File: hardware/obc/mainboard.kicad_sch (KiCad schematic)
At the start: 0 parts

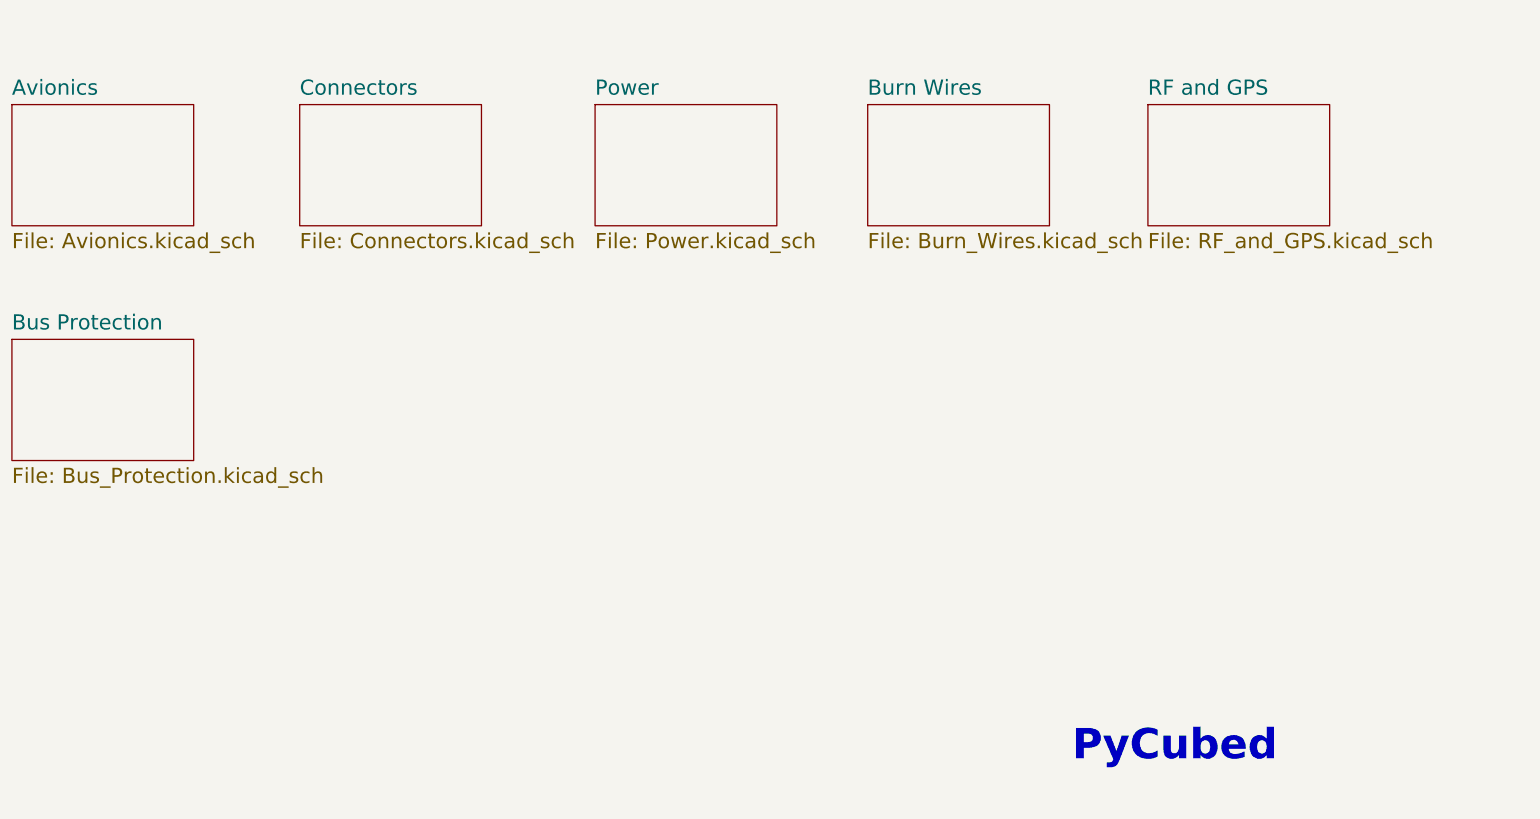
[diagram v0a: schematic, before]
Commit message: obc: Schematic pages to US Letter (except Power)
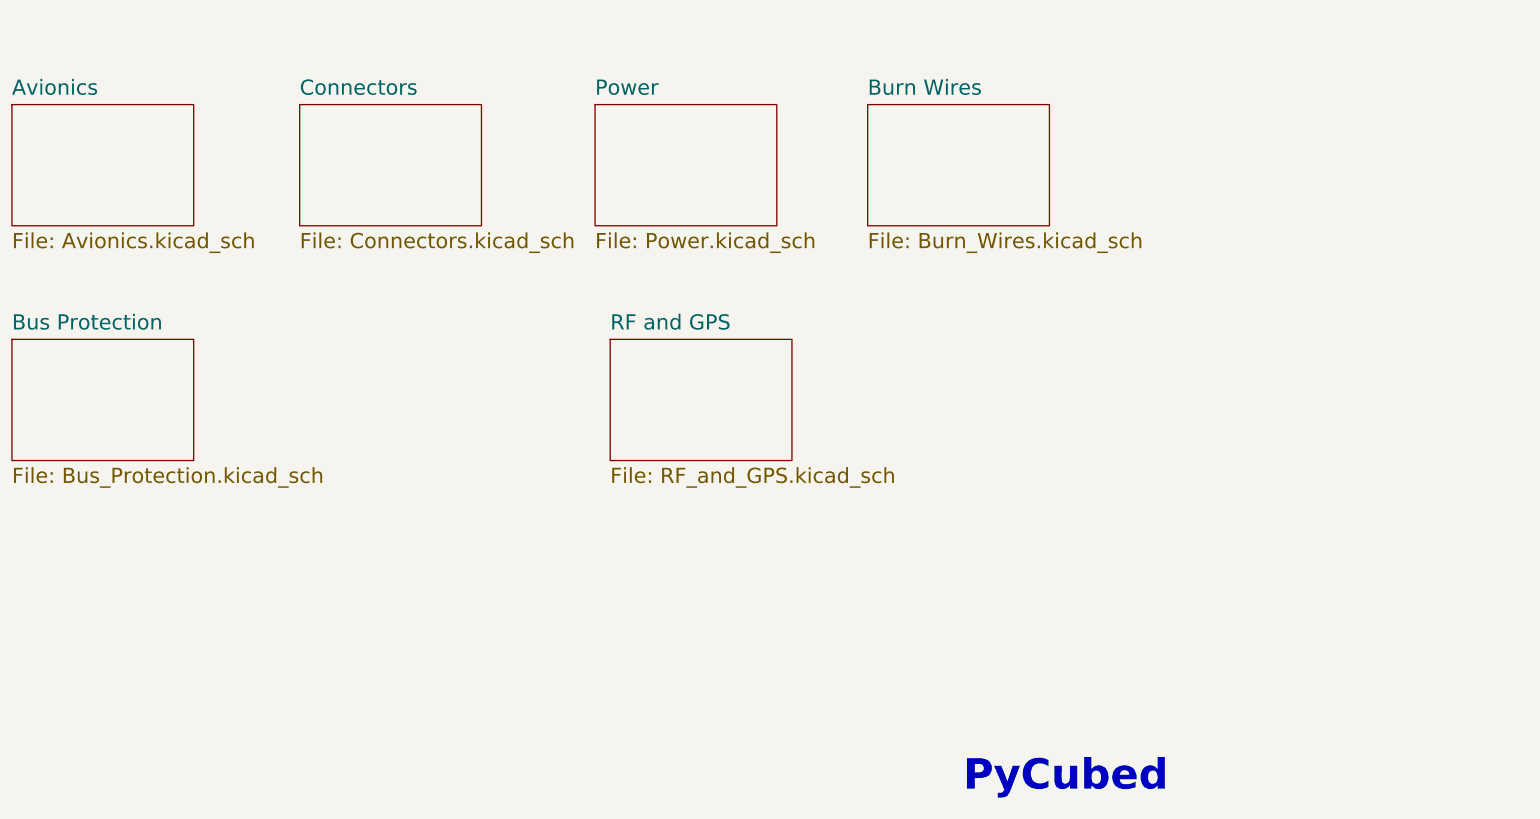
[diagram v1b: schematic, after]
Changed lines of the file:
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@@
 	(generator "eeschema")
 	(generator_version "8.0")
-	(paper "A4")
+	(paper "USLetter")
 	(title_block
 		(title "PyCubed Mainboard")
@@
 	(text "PyCubed"
 		(exclude_from_sim no)
-		(at 212.09 177.8 0)
+		(at 193.802 182.88 0)
 		(effects
 			(font
@@
 	)
 	(sheet
-		(at 224.79 67.31)
+		(at 134.62 106.68)
 		(size 30.48 20.32)
 		(fields_autoplaced yes)
@@
 		)
 		(property "Sheetname" "RF and GPS"
-			(at 224.79 65.9634 0)
+			(at 134.62 105.3334 0)
 			(effects
 				(font
@@
 		)
 		(property "Sheetfile" "RF_and_GPS.kicad_sch"
-			(at 224.79 88.7226 0)
+			(at 134.62 128.0926 0)
 			(effects
 				(font

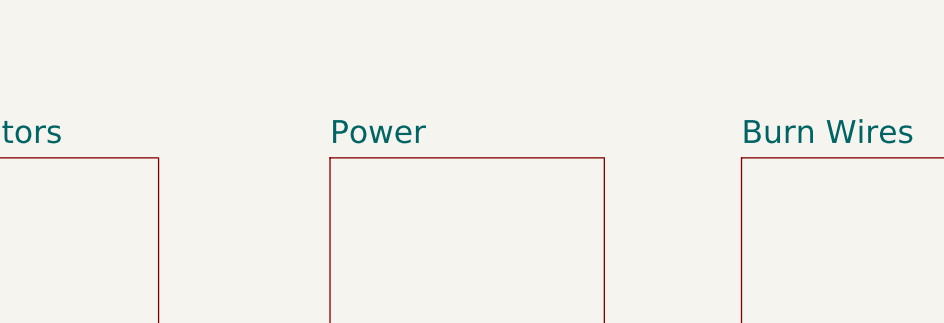
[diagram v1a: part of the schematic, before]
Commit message: obc: schematic editing and footprint development
Deleted irrelevant SD-related circuits and pins. Created new & modified existing connector and inductor footprints. Added new components (Bat Charger, High-Rel Connector, etc.)
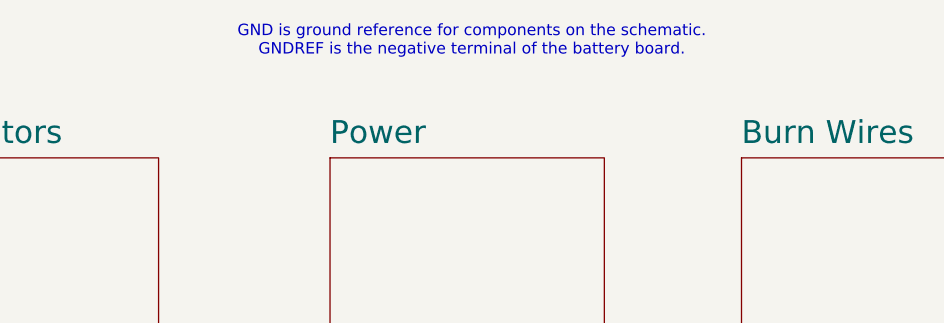
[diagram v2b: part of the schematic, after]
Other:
- note added: "GND is ground reference for components on the schematic. GNDREF is the negative terminal of the battery board."
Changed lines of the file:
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@@
 		(company "Max Holliday")
+	)
+	(text "GND is ground reference for components on the schematic. \nGNDREF is the negative terminal of the battery board."
+		(exclude_from_sim no)
+		(at 147.828 54.356 0)
+		(effects
+			(font
+				(size 1.27 1.27)
+			)
+		)
 	)
 	(text "PyCubed"

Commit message: obc: power connection cleanup
Decreased track length to vias and centered all vias in pad. Updated schematic title blocks, edited 3D models.
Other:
- company: Max Holliday -> Ruchir Kavulli, Michael Lyle
- title: PyCubed Mainboard -> Obi Wan Komputer
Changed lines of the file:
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@@
 	(paper "USLetter")
 	(title_block
-		(title "PyCubed Mainboard")
-		(date "2021-06-09")
-		(rev "v05c")
-		(company "Max Holliday")
+		(title "Obi Wan Komputer")
+		(date "2024-06-07")
+		(rev "vA")
+		(company "Ruchir Kavulli, Michael Lyle")
+		(comment 1 "Derived from PyCubed Mainboard v5")
 	)
 	(text "GND is ground reference for components on the schematic. \nGNDREF is the negative terminal of the battery board."

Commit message: obc: test traces for high priority signals
Preliminary trace creation for high priority signals.
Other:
- title: Obi Wan Komputer -> Obi Wan Computer
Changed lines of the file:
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@@
 	(paper "USLetter")
 	(title_block
-		(title "Obi Wan Komputer")
+		(title "Obi Wan Computer")
 		(date "2024-06-07")
 		(rev "vA")

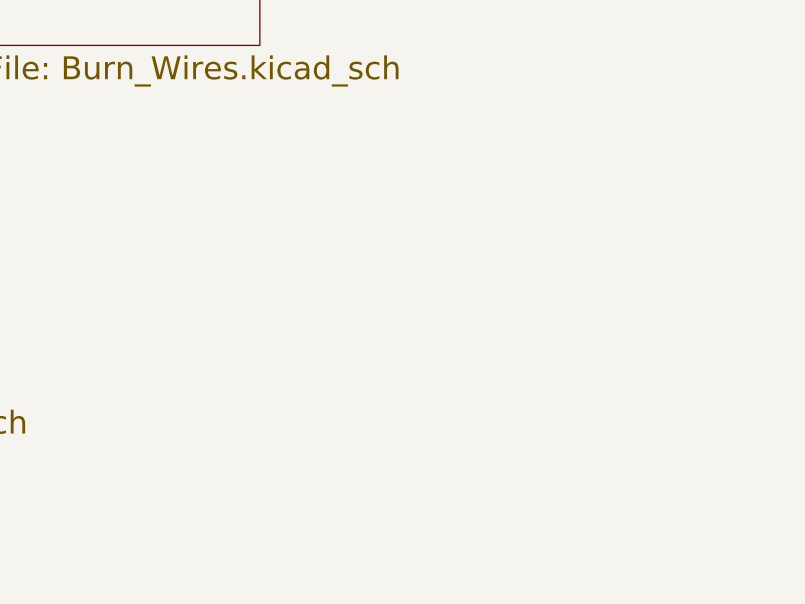
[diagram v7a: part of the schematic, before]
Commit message: OBC; Added another solar charger
- completed all RP2350B decoupling
- added all footprints for new parts
- created a new sheet for all solar charging components
	- added another solar chager to accomadate more voltage from solar pannels
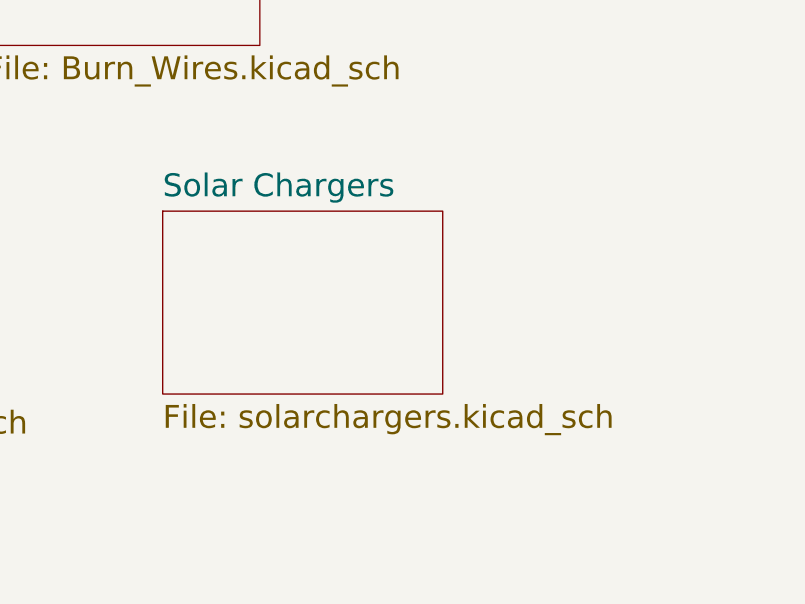
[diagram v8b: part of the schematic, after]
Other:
- added sheet Solar Chargers (solarchargers.kicad_sch)
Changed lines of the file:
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@@
+		)
+	)
+	(sheet
+		(at 197.485 106.045)
+		(size 31.115 20.32)
+		(fields_autoplaced yes)
+		(stroke
+			(width 0.1524)
+			(type solid)
+		)
+		(fill
+			(color 0 0 0 0.0000)
+		)
+		(property "Sheetname" "Solar Chargers"
+			(at 197.485 104.6984 0)
+			(effects
+				(font
+					(size 2.54 2.54)
+				)
+				(justify left bottom)
+			)
+		)
+		(property "Sheetfile" "solarchargers.kicad_sch"
+			(at 197.485 127.4576 0)
+			(effects
+				(font
+					(size 2.54 2.54)
+				)
+				(justify left top)
+			)
+		)
+		(instances
+			(project "mainboard"
+				(path "/e3ac22ea-6806-4807-a025-571315789c25"
+					(page "8")
+				)
+			)
 		)
 	)
